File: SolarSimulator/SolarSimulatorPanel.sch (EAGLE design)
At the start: 79 parts, among them U1 Red Driver, U2 Green Driver, U3 Blue Driver, X1 MKDSN1,5/2-5,08

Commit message: Beeeg cleanup. Converted passives to RCL custom, cleaned up switcher layout, started the Big Stitch, and cleaned up where possible. Left to do: LED footprint cleanup, and routing to dump their heat to a ground pad below them.
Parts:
- added R12, R13, R14: 10k, oresat-rcl:R-US_0603-B-NOSILK
- C10, C3, C7: value (none) -> 10n 25V; device rcl:C-EUC0402K -> oresat-rcl:C-EU0603-B-NOSILK
- C11, C4, C5: device rcl:C-EUC1206 -> oresat-rcl:C-EU1206-B
- C12, C2, C9: value (none) -> 100n 25V; device rcl:C-EUC0603K -> oresat-rcl:C-EU0603-B-NOSILK
- R1, R4, R5: device rcl:R-US_R1206 -> oresat-rcl:R-US_0603-B-NOSILK
- R11: device solarsim:0402RESISTOR -> oresat-rcl:R-US_0603-B-NOSILK
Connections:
- net N$28 renamed GREEN-RTN
- net N$3 renamed RED-OUT
- net N$54 renamed BLUE-RTN
- net N$55 renamed BLUE-OUT
- net N$79 renamed RED-RTN
- net N$80 renamed GRN-OUT
- removed net N$47: R11.2, TB1.+5V
- removed net N$51: R10.A, TB1.A0
- removed net N$58: R9.A, TB1.A1
- removed net N$59: R8.A, TB1.A2
- removed net N$93: R7.A, TB1.A3
- new net +5V: R11.1, R12.1, R13.1, R14.1, TB1.+5V
- new net N$60: R14.2, R7.E, TB1.A3
- new net N$61: R13.2, R8.E, TB1.A2
- new net N$62: R12.2, R9.E, TB1.A1
- net GND: now also R10.A, R7.A, R8.A, R9.A
- net N$91: now also R11.2, TB1.A0; no longer R11.1, R7.E, R8.E, R9.E
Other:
- note added: "BLUE"
- note added: "GREEN"
- note added: "Powered off USB"
- note added: "RED"
- note added: "Thermistors"
- moved on the sheet: BLUE1, BLUE10, BLUE11, BLUE12, BLUE13, BLUE14, BLUE15, BLUE2, BLUE3, BLUE4, BLUE5, BLUE6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

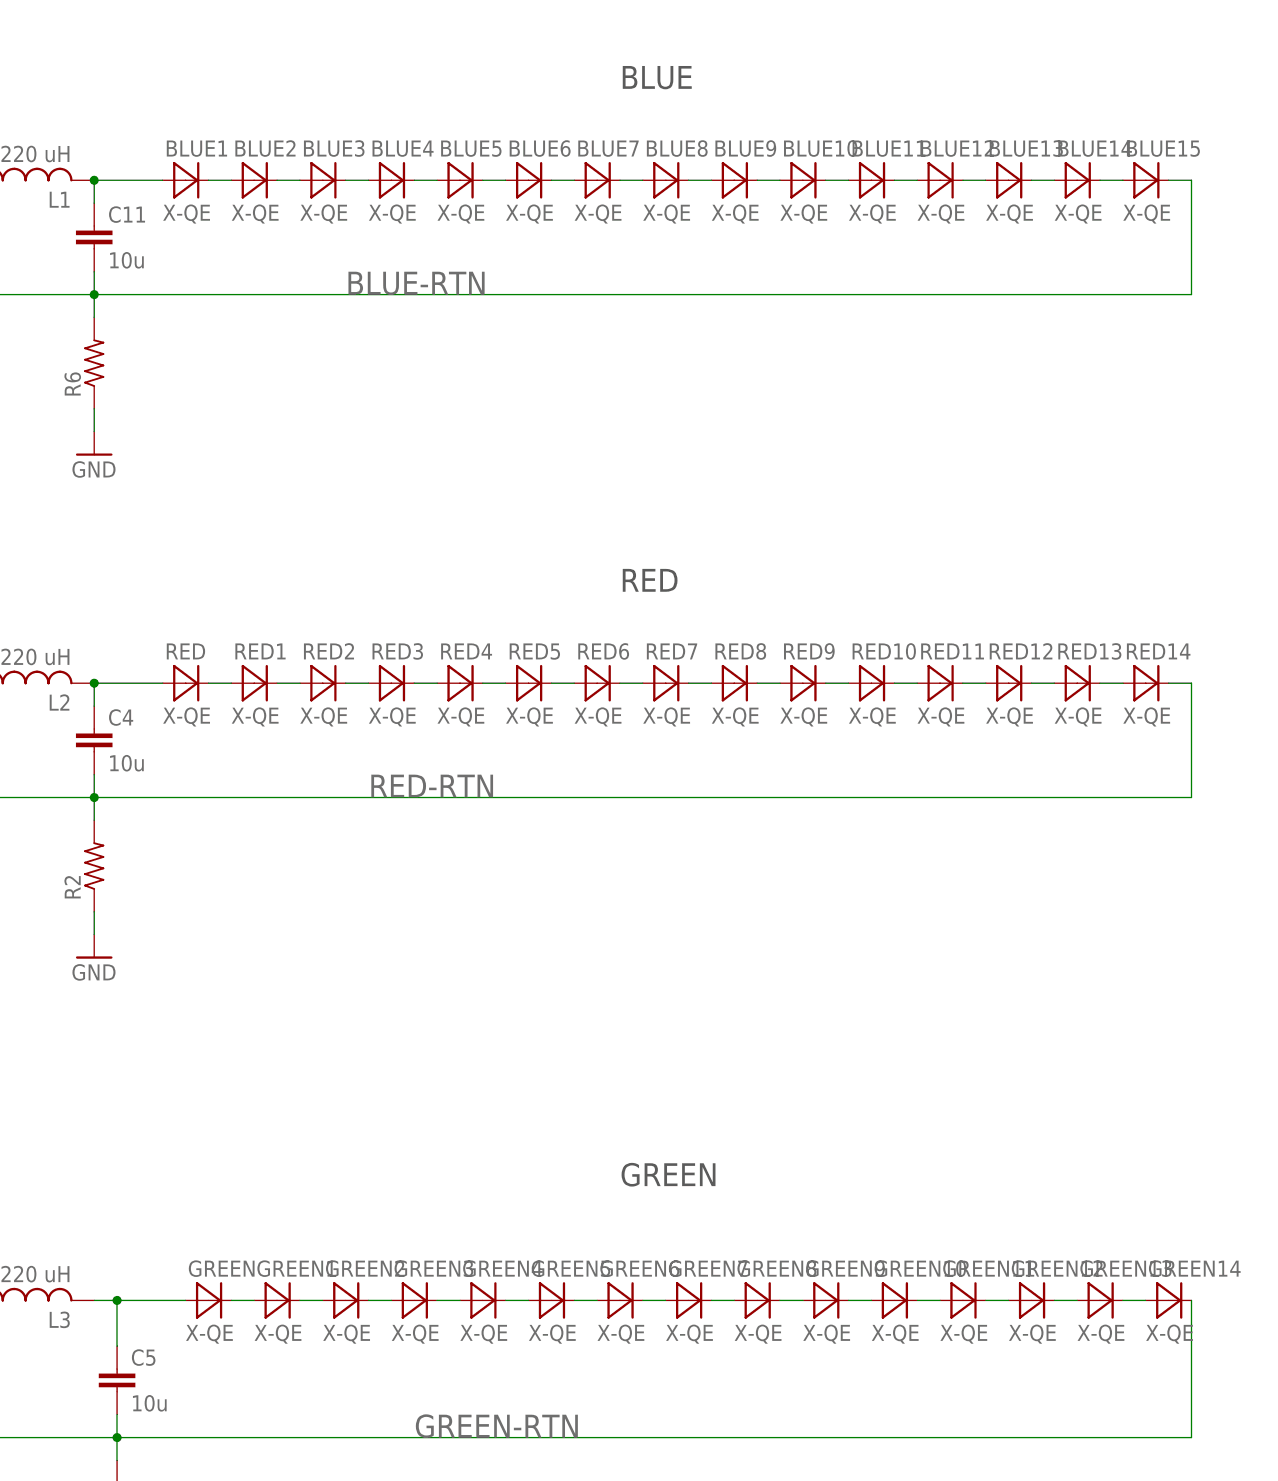
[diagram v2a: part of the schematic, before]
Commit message: Copper cleanup of solar simulator board. Left LEDs about where they were as much as possible, moved origins ot center on LEDs, tried to sink as much heat to the bottom layer as possible.
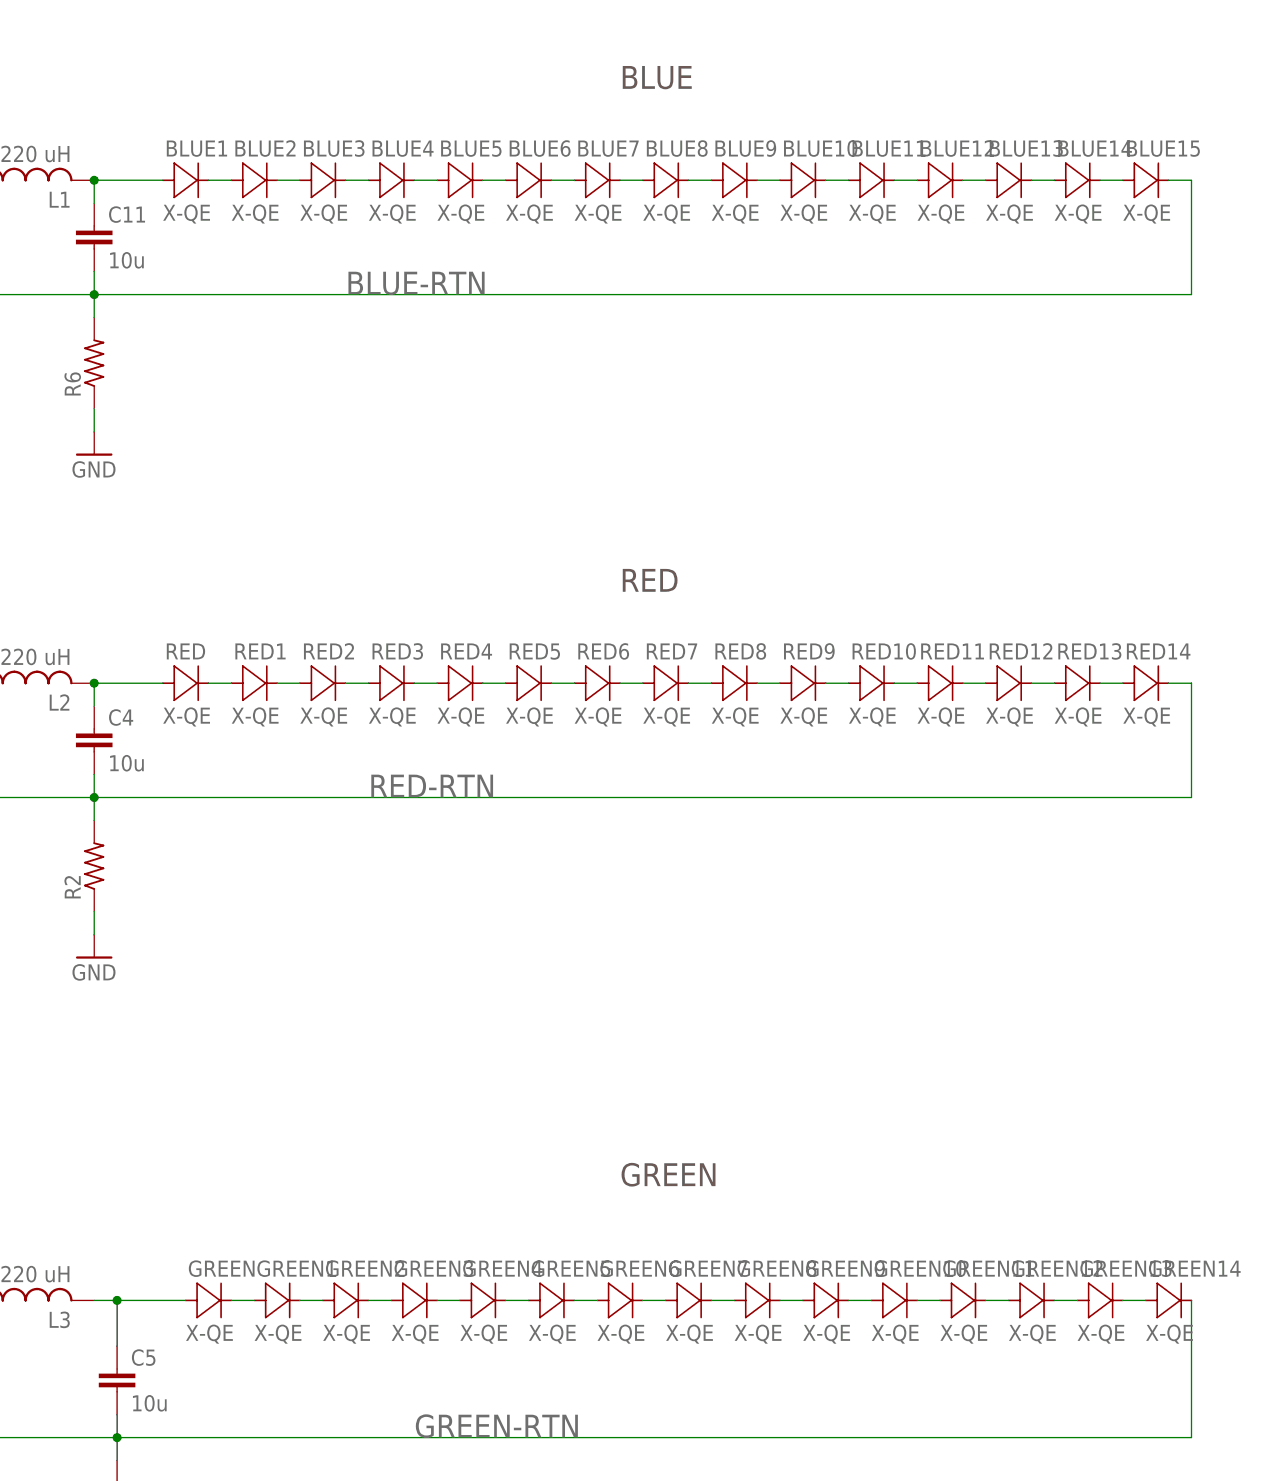
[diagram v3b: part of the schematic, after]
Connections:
- net N$24 renamed N$8SHSHOW
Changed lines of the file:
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@@
 </segment>
 </net>
-<net name="N$24" class="0">
+<net name="N$8SHSHOW" class="0">
 <segment>
 <pinref part="BLUE9" gate="G$1" pin="C"/>

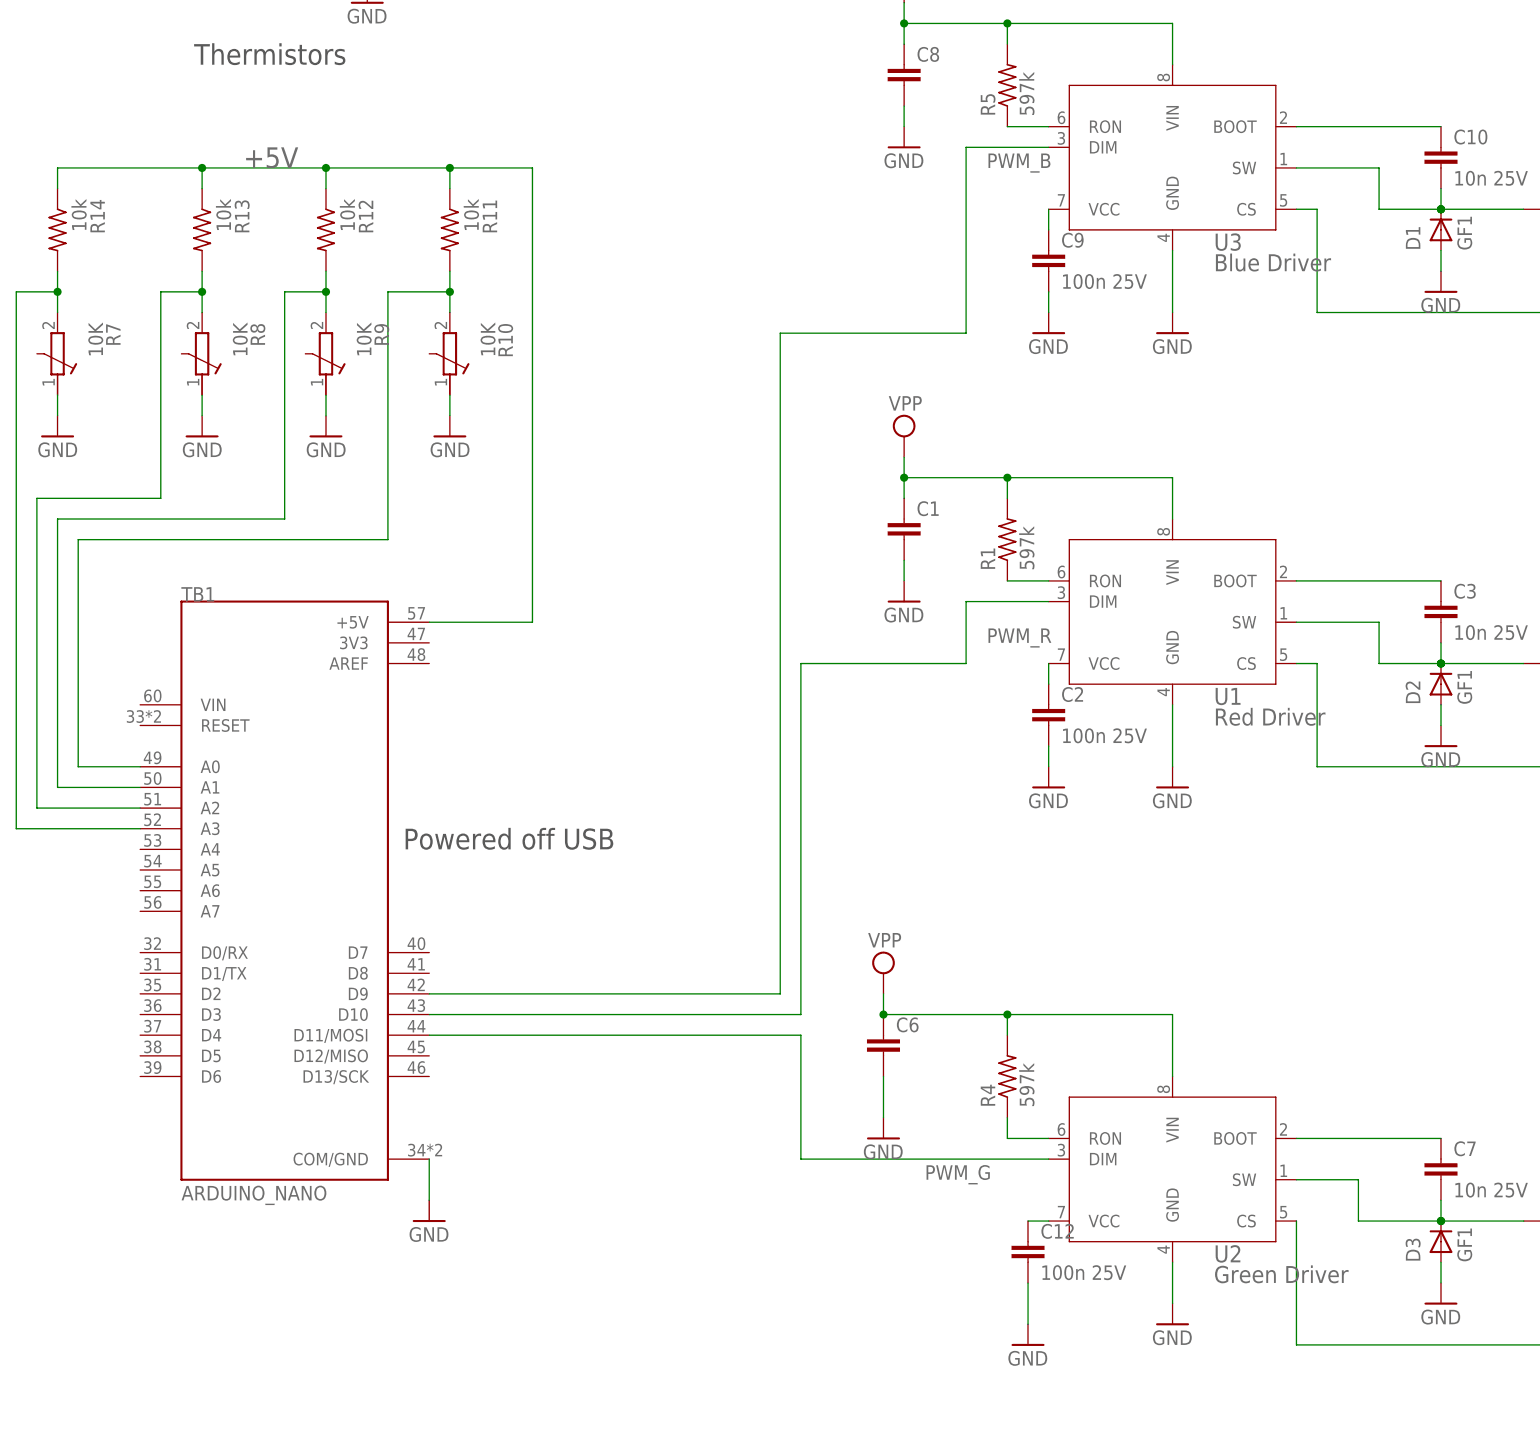
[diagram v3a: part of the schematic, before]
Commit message: Big massive shrinkification and OCDification after discussing board with Catie. Moved the Nano off to the overhang area so we could arbitrarily reduce the distance to the solar cell, added two extra holes to get better thermal contact ot the aluminum panel, re-did the DXF, and scrunched everything together.
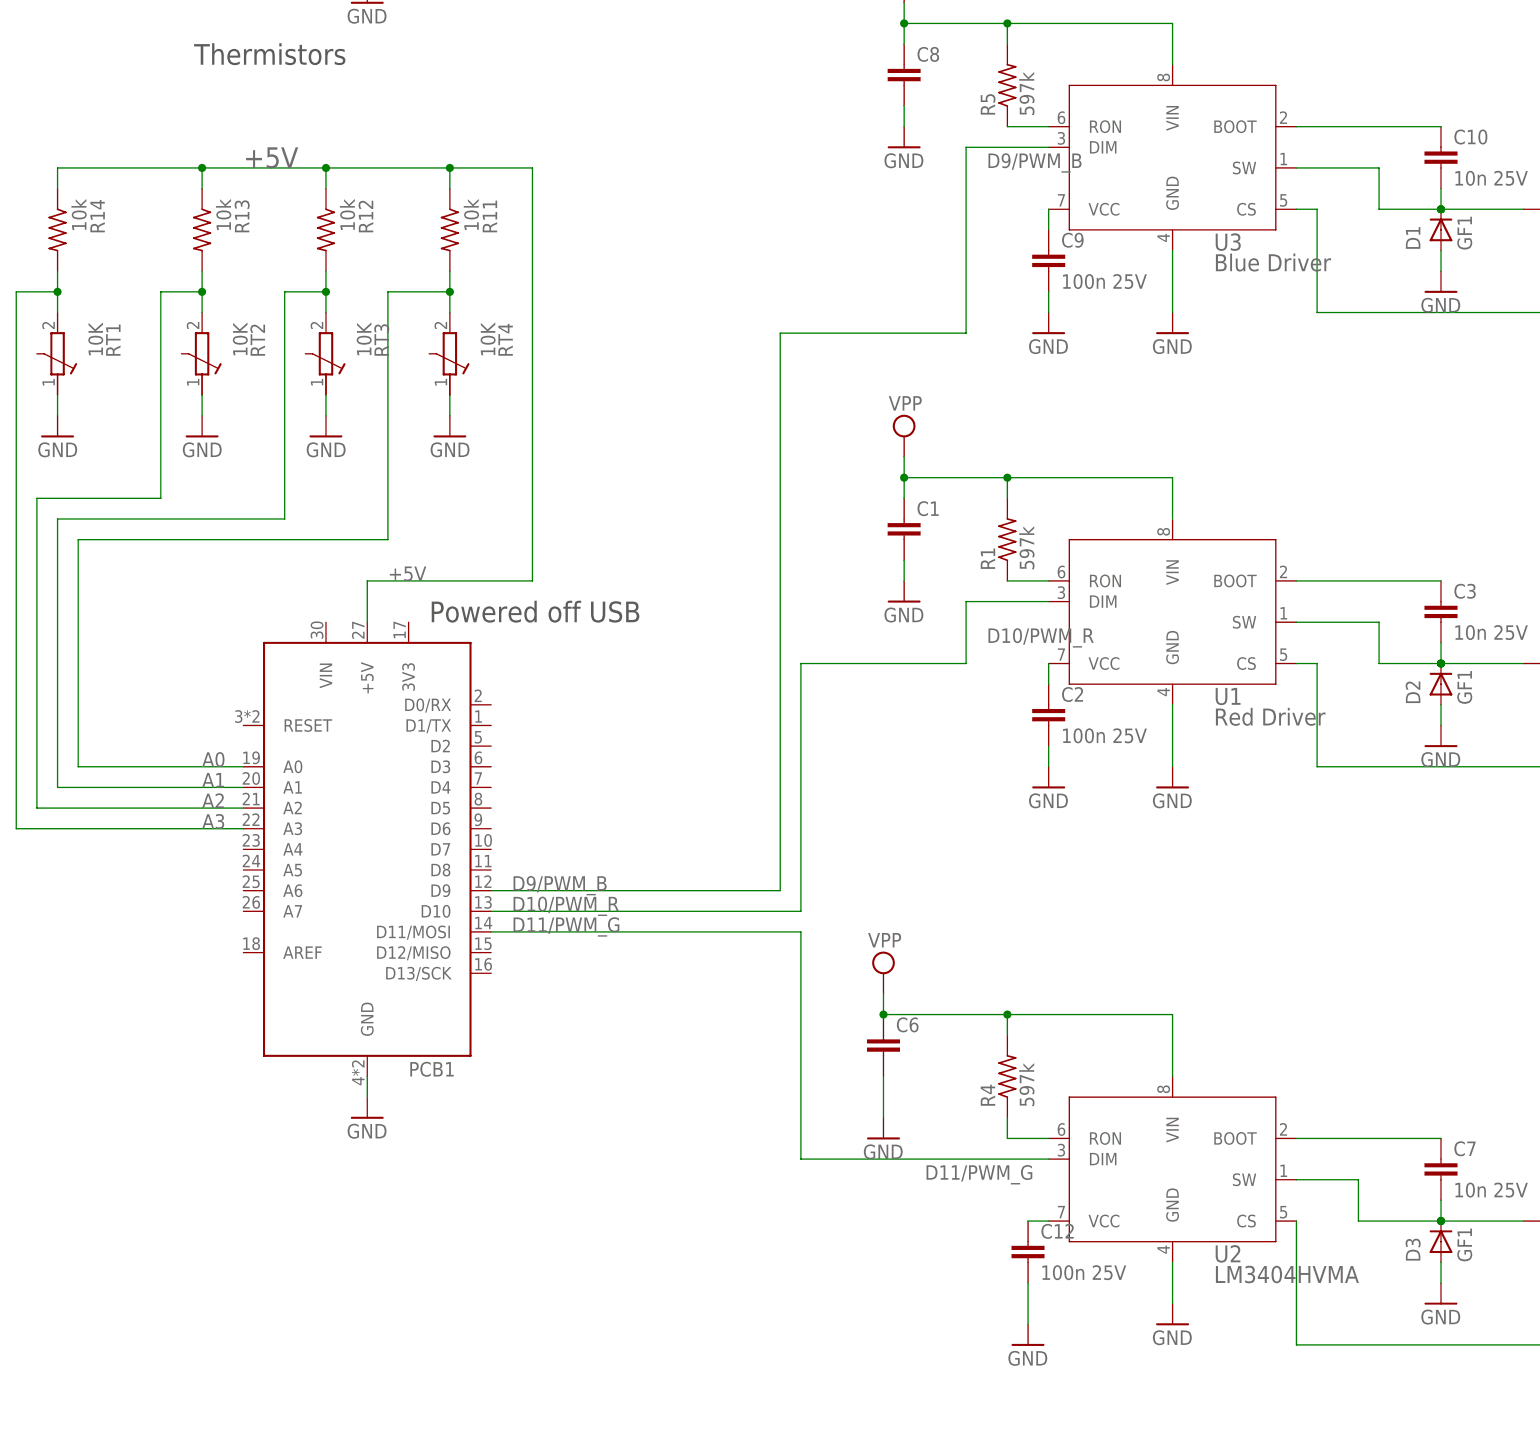
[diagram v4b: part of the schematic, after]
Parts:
- removed TB1: ARDUINO_NANO, ARDUINO_NANO:ARDUINO_NANO
- added PCB1: ARDUINO_NANO, ARDUINO_NANO:ARDUINO_NANO
- L1, L2, L3: MFR (none) -> Bourns; MPN (none) -> SRR1260-221K
- U2: value Green Driver -> LM3404HVMA
- renumbered R10 to RT4, R7 to RT1, R8 to RT2, R9 to RT3
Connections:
- removed net N$60: R14.2, RT1.E, TB1.A3
- removed net N$61: R13.2, RT2.E, TB1.A2
- removed net N$62: R12.2, RT3.E, TB1.A1
- removed net N$91: R11.2, RT4.E, TB1.A0
- removed net PWM_B: TB1.D9, U3.DIM
- removed net PWM_G: TB1.D11/MOSI, U2.DIM
- removed net PWM_R: TB1.D10, U1.DIM
- new net A0: PCB1.A0, R11.2, RT4.E
- new net A1: PCB1.A1, R12.2, RT3.E
- new net A2: PCB1.A2, R13.2, RT2.E
- new net A3: PCB1.A3, R14.2, RT1.E
- new net D10/PWM_R: PCB1.D10, U1.DIM
- new net D11/PWM_G: PCB1.D11/MOSI, U2.DIM
- new net D9/PWM_B: PCB1.D9, U3.DIM
- net +5V: now also PCB1.+5V; no longer TB1.+5V
- net GND: now also PCB1.GND; no longer TB1.COM/GND
